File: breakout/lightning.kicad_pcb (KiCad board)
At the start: 2 copper layers, 27.9 x 19.3 mm, 16 parts, among them J1 GS2, J2 GS3, J3 CONN_01X07, U1 AS3935

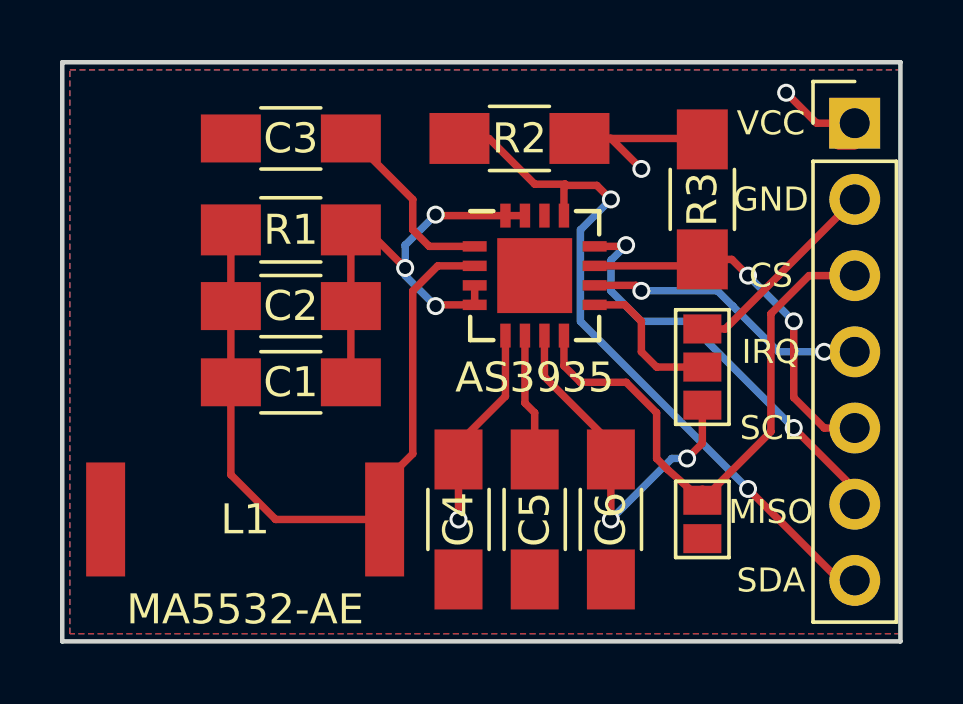
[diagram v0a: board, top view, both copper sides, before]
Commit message: [enh] Enhance silkscreen indications and traces layout
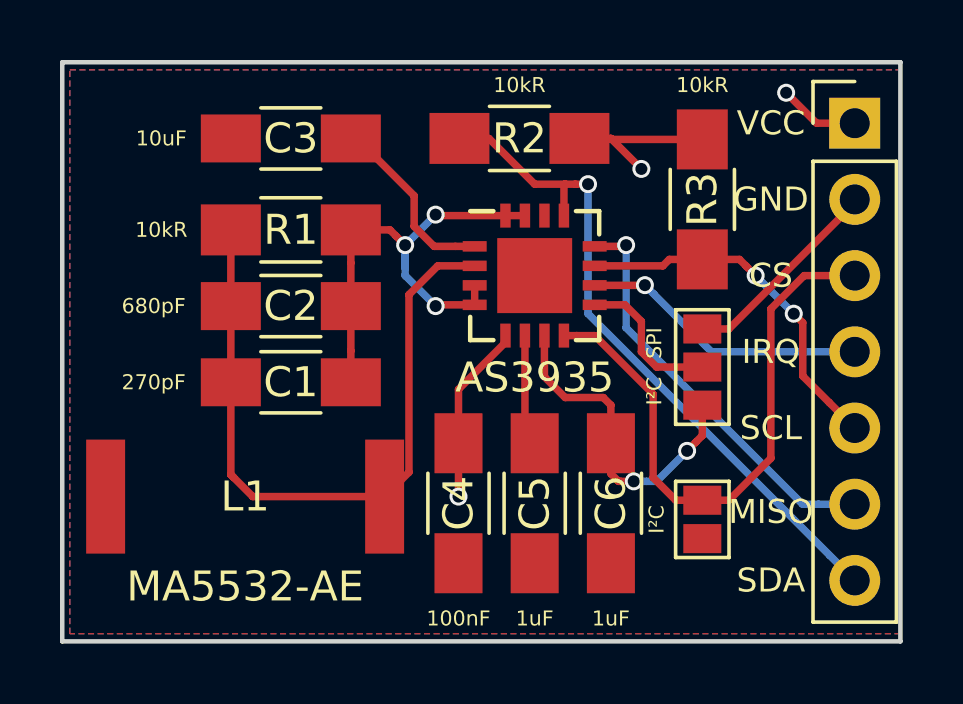
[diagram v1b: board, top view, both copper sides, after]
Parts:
- R1, R2, R3: value 10k -> 10kR
- moved L1 0.76 mm to (148.1, 100.3)
- moved C4 0.54 mm to (155.2, 100.6)
- moved C5 0.54 mm to (157.7, 100.6)
- moved C6 0.54 mm to (160.3, 100.6)
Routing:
- net VCC: track 29.7 -> 25.3 mm
- net Net-(C1-Pad1): track 25.3 -> 23.9 mm
- net /SDA/MOSB: track 24.2 -> 22.9 mm, vias 2 -> 1
- net Net-(C5-Pad1): track 4.26 -> 3.72 mm
- net /MISO: track 14.2 -> 13.9 mm, vias 2 -> 1
- net /IRQ: vias 2 -> 1
